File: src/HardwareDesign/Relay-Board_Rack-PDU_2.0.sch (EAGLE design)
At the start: 68 parts, among them IC1 ULN2803A, IC3 TS432ILT, T1 750370228

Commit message: working on Rev2.0
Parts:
- removed CON1: (no value), ds_con:CON-2X7
- added 3V3DC, 5VDC, GND, GND-3, GND-5, SW3, SW5, VFB3, VFB5: TP, ds_passive:TP
- added C1, C2: 100nF, ds_passive:C-0402
- added C36, C40, C42, C48, C49, C51: 100nF, ds_passive:C0402
- added C43, C52: 33pF, ds_passive:C0402
- added C44, C45: 22uF 25V, ds_passive:C-1206
- added C46, C47, C53, C57: 22uF - 10V, ds_passive:C-1206
- added IC2: MCP23017-E/ML, ds_ic_peripherals:MCP23017-E/ML
- added IC5: MP2315S, ds_ic_vreg:MP2315TSOT23-8
- added IC7: MP2315GJ-Z, ds_ic_vreg:MP2315TSOT23-8
- added L1: 4.9uH, ds_passive:L
- added L3: 4.2uH, ds_passive:L
- added R29, R45: 100K, ds_passive:R0402
- added R30, R31: 499K, ds_passive:R0402
- added R32, R37: 7.5K, ds_passive:R0402
- added R33: 9.09K, ds_passive:R0402
- added R34, R41: 10R, ds_passive:R0402
- added R35: 20K, ds_passive:R0402
- added R36, R43: 40.2K, ds_passive:R0402
- added R42: 33K, ds_passive:R0402
- added R44: 12.7K, ds_passive:R0402
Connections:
- removed net I_MEA/TX: CON1.4
- removed net VMEA/RX: CON1.3
- new net EXP_RST: IC2.!RESET
- new net I2C_SCL: IC2.SCL
- new net I2C_SDA: IC2.SDA
- new net N$14: IC7.BST, R34.2
- new net N$16: IC7.FB, R35.1
- new net N$17: C51.2, IC7.SW, L1.1, SW5.P$1
- new net N$18: C51.1, R34.1
- new net N$19: IC7.EN, R31.2
- new net N$21: C49.1, IC7.VCC, R29.1
- new net N$37: C52.2, R35.2, R36.2, R37.1, VFB5.P$1
- new net N$38: IC5.BST, R41.2
- new net N$39: IC5.FB, R42.1
- new net N$40: C42.2, IC5.SW, L3.1, SW3.P$1
- new net N$41: C42.1, R41.1
- new net N$42: C43.2, R42.2, R43.2, R44.1, VFB3.P$1
- new net N$43: IC5.EN, R30.2
- new net N$44: C40.1, IC5.VCC, R45.1
- new net N$45: IC7.AAM, R29.2, R33.1
- new net N$46: IC5.AAM, R32.1, R45.2
- net +12V: now also C36.1, C44.1, C45.1, C48.1, IC5.IN, IC7.IN, R30.1, R31.1; no longer CON1.14
- net +3V3: now also 3V3DC.P$1, C1.1, C2.1, C43.1, C47.1, C57.1, IC2.VDD, L3.2, R43.1; no longer CON1.1
- net +5V: now also 5VDC.P$1, C46.1, C52.1, C53.1, L1.2, R36.1; no longer CON1.2
- net GND: now also C1.2, C2.2, C36.2, C40.2, C44.2, C45.2, C46.2, C47.2, C48.2, C49.2, C53.2, C57.2, GND-3.P$1, GND-5.P$1, GND.P$1, IC2.A0, IC2.A1, IC2.A2, IC2.VSS, IC5.GND, IC7.GND, R32.2, R33.2, R37.2, R44.2; no longer CON1.13
- net REL_0: now also IC2.IO1.0; no longer CON1.12
- net REL_1: now also IC2.IO1.1; no longer CON1.11
- net REL_2: now also IC2.IO1.2; no longer CON1.10
- net REL_3: now also IC2.IO1.3; no longer CON1.9
- net REL_4: now also IC2.IO1.4; no longer CON1.8
- net REL_5: now also IC2.IO1.5; no longer CON1.7
- net REL_6: now also IC2.IO1.6; no longer CON1.6
- net REL_7: now also IC2.IO1.7; no longer CON1.5
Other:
- note added: "3.3V DC-DC CONVERTER"
- note added: "5V DC-DC CONVERTER"
- note added: "IO DRIVER"
- note removed: "DRIVER CONNECTOR"
- moved on the sheet: IC1, R1, R2, R3, R4, R5, R6, R7, R8

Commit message: working on Rev2.0
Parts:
- removed 3V3DC, SW5, VFB3, VFB5: TP, ds_passive:TP
- removed BR1: DBLS207G, ds_active:DBLS207G
- removed C45: 22uF 25V, ds_passive:C-1206
- removed C46, C47, C53, C57: 22uF - 10V, ds_passive:C-1206
- removed C51: 100nF, ds_passive:C0402
- removed C52: 33pF, ds_passive:C0402
- removed CM1: 20mH CM CHOKE, ds_trafo:WE-CMB_XS_744821120
- removed D15: MRA4007T3G, Diodes:SS12
- removed D16: STPS5H100B, ds_active:STPS5H100B
- removed D17, D18, D19: BAT41ZFILM, diode:CGRM4001-G
- removed D20: MMSZ5248B-V-GS08, Diodes-2:BZG03C240-HM3-08
- removed F2: 696101000002, Wurth_Connectors_WR-FSH:696101000002
- removed L3: 4.2uH, ds_passive:L
- removed REL1, REL2, REL3, REL4, REL5, REL6, REL7, REL8: G2RL-1A-E_DC12, ds_passive:G2RL-1A-E_DC12
- removed RV1: B72210S0321K101, Wurth_EMC Components_WE-VD:WE-VD_10MM_820412001
- removed T1: 750370228, ds_trafo:750370228
- added 12VDC, 3VDC, 3VFB, 5VFB, SW: TP, ds_passive:TP
- added AC/DC1: (no value), ds_trafo:IRM_10_12
- added AC_L, AC_N: (no value), con-wago-500:W237-102
- added C10, C13: 100uF, ds_passive:CPOL
- added C11, C12: 33pF, ds_passive:C0402
- added C27, C28, C29, C30, C31, C32, C37, C38, C39, C41, C50, C54, C55, C56: 33nF, ds_passive:C-1206
- added C3, C4, C6, C7, C8, C9: 100nF, ds_passive:C0402
- added C33, C34: 100nF, ds_passive:C-0402
- added C5: 10uF 16V, ds_passive:C-1206
- added D10, D9: S1M, diode:S1M
- added D11: 9.1V 1W, diode:ZENER-DIODESMB
- added IC10, IC11, IC12, IC14, IC16, IC6, IC8: HLW8032, ds_ic_peripherals:HLW8032
- added IC9: SN74HC151PWR, ds_ic_logic:SN74HC151PWR
- added J1: 687320124422, Wurth_Connectors_WR-FPC:6873XX124422_687320124422
- added K1, K2, K3, K4, K5, K6, K7, K8: G2RL-1A-E_DC12, ds_passive:G2RL-1A-E_DC12
- added OPT1: TLP291-4, ds_ic_peripherals:TLP291-4(GB-TP,E)1
- added R100, R101, R102, R103, R116, R117, R118, R119, R38, R39, R46, R47, R52, R53, R54, R55, R68, R69, R70, R71, R76, R77, R78, R79, R84, R85, R86, R87: 470K, ds_passive:R1206
- added R104, R113, R114, R120, R40, R48, R49, R50, R56, R65, R66, R72, R73, R74, R80, R81, R82, R88, R97, R98: 1K 1%, ds_passive:R1206
- added R11: 40.2K, ds_passive:R0402
- added R115, R25, R26, R27, R28, R51, R67, R75, R83, R99: 0.002R 1%, ds_passive:R2512
- added R12: 7.5K, ds_passive:R0402
- added R57, R58, R59: JP, ds_passive:R0402
- added R60: 470K 1W, ds_passive:R2512
- added R61, R62: 100R 1W, ds_passive:R2512
- added R63, R64, R89, R90: 4x1K 1206, Resistor Array:742C083103JP
- added R91, R92: 0R, ds_passive:R0402
- added R93: 4x10K 1206, Resistor Array:742C083103JP
- added R94: 100K, ds_passive:R0402
- added R95: 10K, ds_passive:R0402
- added Z1: SMAJ15A, 52101-101-REV-A_v16:SUPRESSOR_TVS-UD-SMAJ
- C1, C2: value 100nF -> 22uF 25V; device ds_passive:C-0402 -> ds_passive:C-1206
- C14: value MP2104K27C3R6LC 100nF 275V -> 22uF - 10V; device ds_passive:C -> ds_passive:C-1206
- C15, C17: value KM150M400G160A 15uF 400V -> 22uF - 10V; device Capacitor:C-POL_RADIAL-25MM-DIA -> ds_passive:C-1206
- C16: value 1nF 630V -> 100uF; device ds_passive:C-1206 -> ds_passive:CPOL
- C18: value 470uF 25V -> 22uF - 10V; device Capacitor:C-POL_RADIAL-11MM-DIA -> ds_passive:C-1206
- C19: value 100uF 25V -> 100nF; device Capacitor:C-POL_RADIAL-11MM-DIA -> ds_passive:C-0402
- C20: value 1uF 25V -> 100nF; device ds_passive:C-0805 -> ds_passive:C-0402
- C21: value 10nF 50V -> 470nF 630V; device ds_passive:C-0805 -> ds_passive:C-2225
- C22: value 2.2nF 50V -> 470uF 25V; device ds_passive:C-0603 -> ds_passive:CPOL
- C23: value 33nF 16V -> 10uF 16V; device ds_passive:C-0603 -> ds_passive:C-1206
- C24: value 220pF -> 33nF; device ds_passive:C-0805 -> ds_passive:C-1206
- C25: value 33uF 35V -> 33nF; device Capacitor:C-POL_RADIAL-11MM-DIA -> ds_passive:C-1206
- C26: value 2.2nF 250VAC -> 33nF; device ds_passive:C102-1KV -> ds_passive:C-1206
- C36, C40, C42, C48, C49: value 100nF -> 33nF; device ds_passive:C0402 -> ds_passive:C-1206
- C43: value 33pF -> 33nF; device ds_passive:C0402 -> ds_passive:C-1206
- C44: value 22uF 25V -> 33nF
- IC1: value ULN2803A -> MP2315GJ-Z; device ds_ic_peripherals:ULN2803 -> ds_ic_vreg:MP2315TSOT23-8
- IC2: value MCP23017-E/ML -> MP2315S; device ds_ic_peripherals:MCP23017-E/ML -> ds_ic_vreg:MP2315TSOT23-8
- IC3: value TS432ILT -> ULN2803A; device ds_ic_vreg:TS432ILT -> ds_ic_peripherals:ULN2803
- IC4: value (none) -> MCP23017-E/ML; device ds_ic_peripherals:VIPER35HD -> ds_ic_peripherals:MCP23017-E/ML
- IC5: value MP2315S -> BA50BC0FP-E2; device ds_ic_vreg:MP2315TSOT23-8 -> ds_ic_vreg:L4941BDT
- IC7: value MP2315GJ-Z -> HLW8032; device ds_ic_vreg:MP2315TSOT23-8 -> ds_ic_peripherals:HLW8032
- L2: value 3.3uH SD43-332ML -> 4.2uH; device 52101-101-REV-A_v16:INDUCTOR-BOURNS_SRN8040 -> ds_passive:L
- OPT2: value SFH6106-2T -> TLP291-4; device ds_ic_peripherals:SFH6106-3SMD-4_SFH610X_VIS-M -> ds_ic_peripherals:TLP291-4(GB-TP,E)1
- R1, R2: value 330R 1W -> 499K; device ds_passive:R1206 -> ds_passive:R0402
- R10: value 0R -> 33K; device ds_passive:R0805 -> ds_passive:R0402
- R13: value 220K 5% 0.33W 200V -> 40.2K; device ds_passive:R1206 -> ds_passive:R0402
- R14: value 1K -> 12.7K; device ds_passive:R0603 -> ds_passive:R0402
- R15: value 12K -> 0R; device ds_passive:R0603 -> ds_passive:R0805
- R16: value 82K -> 0R; device ds_passive:R0603 -> ds_passive:R0805
- R17: value 130K 1% -> 330R 1W; device ds_passive:R0603 -> ds_passive:R1206
- R18: value 15K 1% -> 330R 1W; device ds_passive:R0603 -> ds_passive:R1206
- R19: value 4.7R 1% -> 330R 1W; device ds_passive:R0603 -> ds_passive:R1206
- R20: value 330K 1% -> 330R 1W; device ds_passive:R0603 -> ds_passive:R1206
- R21: value 133K 1% -> 330R 1W; device ds_passive:R0603 -> ds_passive:R1206
- R22: value 30K 1% -> 330R 1W; device ds_passive:R0603 -> ds_passive:R1206
- R23: value 47K 1% -> 330R 1W; device ds_passive:R0603 -> ds_passive:R1206
- R24: value 220R -> 330R 1W; device ds_passive:R0805 -> ds_passive:R1206
- R29: value 100K -> 0.002R 1%; device ds_passive:R0402 -> ds_passive:R2512
- R3, R5: value 330R 1W -> 100K; device ds_passive:R1206 -> ds_passive:R0402
- R30, R31: value 499K -> 0.002R 1%; device ds_passive:R0402 -> ds_passive:R2512
- R32: value 7.5K -> 0.002R 1%; device ds_passive:R0402 -> ds_passive:R2512
- R33: value 9.09K -> 1K 1%; device ds_passive:R0402 -> ds_passive:R1206
- R34, R41: value 10R -> 1K 1%; device ds_passive:R0402 -> ds_passive:R1206
- R35: value 20K -> 0.002R 1%; device ds_passive:R0402 -> ds_passive:R2512
- R36: value 40.2K -> 470K; device ds_passive:R0402 -> ds_passive:R1206
- R37: value 7.5K -> 470K; device ds_passive:R0402 -> ds_passive:R1206
- R4: value 330R 1W -> 9.09K; device ds_passive:R1206 -> ds_passive:R0402
- R42: value 33K -> 1K 1%; device ds_passive:R0402 -> ds_passive:R1206
- R43: value 40.2K -> 0.002R 1%; device ds_passive:R0402 -> ds_passive:R2512
- R44: value 12.7K -> 470K; device ds_passive:R0402 -> ds_passive:R1206
- R45: value 100K -> 470K; device ds_passive:R0402 -> ds_passive:R1206
- R6: value 330R 1W -> 7.5K; device ds_passive:R1206 -> ds_passive:R0402
- R7: value 330R 1W -> 10R; device ds_passive:R1206 -> ds_passive:R0402
- R8: value 330R 1W -> 20K; device ds_passive:R1206 -> ds_passive:R0402
- R9: value 0R -> 10R; device ds_passive:R0805 -> ds_passive:R0402
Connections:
- removed net AC_LINE: F2.1, REL1.3, REL1.6, REL2.3, REL2.6, REL3.3, REL3.6, REL4.3, REL4.6, REL5.3, REL5.6, REL6.3, REL6.6, REL7.3, REL7.6, REL8.3, REL8.6
- removed net AC_LINE2: C14.2, CM1.1, RV1.2
- removed net DC_RAW: BR1.+, C15.+, C16.1, C17.+, R13.2, T1.6
- removed net EXP_RST: IC2.!RESET
- removed net FB: C22.1, C23.1, IC4.FB, OPT2.3
- new net +12V_MEA: J1.13, R94.1, R95.2
- new net +5V_MEA: C23.1, C5.1, IC10.VDD, IC11.VDD, IC12.VDD, IC14.VDD, IC16.VDD, IC5.VOUT, IC6.VDD, IC7.VDD, IC8.VDD, R63.1, R63.2, R63.3, R63.4, R64.1, R64.2, R64.3, R64.4
- new net 5VFB: 5VFB.P$1, C11.2, R11.2, R12.1, R8.2
- new net AC_L: AC/DC1.AC/L, AC_L-1.KL, AC_L-2.KL, C21.1, K1.3, K1.6, K2.3, K2.6, K3.3, K3.6, K4.3, K4.6, K5.3, K5.6, K6.3, K6.6, K7.3, K7.6, K8.3, K8.6, R60.1
- new net AC_N: AC/DC1.AC/N, AC_N-1.KL, AC_N-2.KL, R57.1, R58.1, R59.1
- new net C13_IN1: R25.2, R33.1, R35.2
- new net C13_IN2: R32.2, R49.1, R51.2
- new net C13_IN3: R31.2, R65.1, R67.2
- new net C13_IN4: R30.2, R81.1, R83.2
- new net C13_IN5: R26.2, R41.1, R43.2
- new net C13_IN6: R27.2, R73.1, R75.2
- new net C13_IN7: R28.2, R97.1, R99.2
- new net C13_IN8: R113.1, R115.2, R29.2
- new net MCP_REL_RST: IC4.!RESET, J1.15
- new net MUX_A: IC4.IO2.0, IC9.A, R93.4
- new net MUX_B: IC4.IO2.1, IC9.B, R93.3
- new net MUX_C: IC4.IO2.2, IC9.C, R93.2
- new net MUX_EN: IC4.IO2.3, IC9.!EN, R93.1
- new net N$1: IC9.Y, R91.1
- new net N$100: C56.1, IC16.VP, R119.2, R120.1
- new net N$3: C21.2, R60.2, R61.1
- new net N$4: IC3.5C, R21.1
- new net N$47: C30.1, IC8.INP, R49.2
- new net N$48: C31.1, IC8.INN, R50.2
- new net N$49: R52.2, R53.1
- new net N$50: R53.2, R54.1
- new net N$51: R54.2, R55.1
- new net N$52: C32.1, IC8.VP, R55.2, R56.1
- new net N$53: OPT2.5, R64.6
- new net N$54: OPT2.7, R64.5
- new net N$59: C36.1, IC10.INP, R65.2
- new net N$60: C37.1, IC10.INN, R66.2
- new net N$61: R68.2, R69.1
- new net N$62: R69.2, R70.1
- new net N$63: R70.2, R71.1
- new net N$64: C38.1, IC10.VP, R71.2, R72.1
- new net N$65: C39.1, IC11.INP, R73.2
- new net N$66: C40.1, IC11.INN, R74.2
- new net N$67: R76.2, R77.1
- new net N$68: R77.2, R78.1
- new net N$69: R78.2, R79.1
- new net N$70: C41.1, IC11.VP, R79.2, R80.1
- new net N$71: C42.1, IC12.INP, R81.2
- new net N$72: C43.1, IC12.INN, R82.2
- new net N$73: R84.2, R85.1
- new net N$74: R85.2, R86.1
- new net N$75: R86.2, R87.1
- new net N$76: C44.1, IC12.VP, R87.2, R88.1
- new net N$83: C48.1, IC14.INP, R97.2
- new net N$84: C49.1, IC14.INN, R98.2
- new net N$85: R100.2, R101.1
- new net N$86: R101.2, R102.1
- new net N$87: R102.2, R103.1
- new net N$88: C50.1, IC14.VP, R103.2, R104.1
- new net N$95: C54.1, IC16.INP, R113.2
- new net N$96: C55.1, IC16.INN, R114.2
- new net N$97: R116.2, R117.1
- new net N$98: R117.2, R118.1
- new net N$99: R118.2, R119.1
- new net RX_CH1: IC6.RX
- new net RX_CH2: IC8.RX
- new net RX_CH3: IC10.RX
- new net RX_CH4: IC12.RX
- new net RX_CH5: IC7.RX
- new net RX_CH6: IC11.RX
- new net RX_CH7: IC14.RX
- new net RX_CH8: IC16.RX
- new net SW3: C9.2, IC2.SW, L2.1, SW3.P$1
- new net SW5: C8.2, IC1.SW, L1.1, SW.P$1
- new net TX_CH1: IC6.TX, OPT1.2
- new net TX_CH2: IC8.TX, OPT1.4
- new net TX_CH3: IC10.TX, OPT1.6
- new net TX_CH4: IC12.TX, OPT1.8
- new net TX_CH5: IC7.TX, OPT2.2
- new net TX_CH6: IC11.TX, OPT2.4
- new net TX_CH7: IC14.TX, OPT2.6
- new net TX_CH8: IC16.TX, OPT2.8
- new net TX_MUX1: IC9.D0, OPT1.16, R89.1
- new net TX_MUX2: IC9.D1, OPT1.14, R89.2
- new net TX_MUX3: IC9.D2, OPT1.12, R89.3
- new net TX_MUX4: IC9.D3, OPT1.10, R89.4
- new net TX_MUX5: IC9.D4, OPT2.16, R90.1
- new net TX_MUX6: IC9.D5, OPT2.14, R90.2
- new net TX_MUX7: IC9.D6, OPT2.12, R90.3
- new net TX_MUX8: IC9.D7, OPT2.10, R90.4
- new net UART0_RX: J1.10
- new net UART0_TX: J1.11, R91.2, R92.2
- net +12V: now also C1.1, C2.1, C3.1, C4.1, IC1.IN, IC2.IN, IC3.COM, K1.8, K2.8, K3.8, K4.8, K5.8, K6.8, K7.8, K8.8, R1.1, R15.1, R16.1, R2.1, R94.2; no longer C36.1, C44.1, C45.1, C48.1, IC1.COM, IC5.IN, IC7.IN, R10.1, R30.1, R31.1, R9.1, REL1.8, REL2.8, REL3.8, REL4.8, REL5.8, REL6.8, REL7.8, REL8.8
- net +3V3: now also 3VDC.P$1, C12.1, C15.1, C18.1, C19.1, C20.1, C33.1, C34.1, IC4.VDD, IC9.VCC, J1.4, J1.5, J1.6, L2.2, R13.1, R89.5, R89.6, R89.7, R89.8, R90.5, R90.6, R90.7, R90.8, R93.5, R93.6, R93.7, R93.8; no longer 3V3DC.P$1, C1.1, C2.1, C43.1, C47.1, C57.1, IC2.VDD, L3.2, R43.1
- net +5V: now also C11.1, C14.1, C17.1, J1.1, J1.2, J1.3, R11.1; no longer C46.1, C52.1, C53.1, R36.1
- net AGND: now also C23.2, C25.2, C26.2, C27.2, C28.2, C29.2, C30.2, C31.2, C32.2, C36.2, C37.2, C38.2, C39.2, C40.2, C41.2, C42.2, C43.2, C44.2, C48.2, C49.2, C5.2, C50.2, C54.2, C55.2, C56.2, D10.A, D11.A, IC10.GND, IC11.GND, IC12.GND, IC14.GND, IC16.GND, IC5.GND, IC6.GND, IC7.GND, IC8.GND, R104.2, R120.2, R40.2, R48.2, R56.2, R57.2, R58.2, R59.2, R72.2, R80.2, R88.2; no longer BR1.-, C15.-, C17.-, C25.-, C26.1, D17.A, D20.A, IC4.BR, IC4.GND, OPT2.4, R22.2, R23.2, T1.3
- net GND: now also AC/DC1.-V, C10.2, C13.2, C14.2, C15.2, C16.2, C17.2, C18.2, C19.2, C3.2, C33.2, C34.2, C4.2, C6.2, C7.2, IC2.GND, IC3.GND, IC4.A0, IC4.A1, IC4.A2, IC4.VSS, IC9.GND, J1.12, J1.14, J1.16, J1.9, J1.Z1, J1.Z2, J1.Z3, J1.Z4, OPT1.11, OPT1.13, OPT1.15, OPT1.9, OPT2.11, OPT2.13, OPT2.15, OPT2.9, R12.2, R14.2, R4.2, R6.2, R95.1, Z1.A; no longer C18.-, C19.-, C26.2, C36.2, C40.2, C44.2, C45.2, C46.2, C47.2, C48.2, C49.2, C53.2, C57.2, IC2.A0, IC2.A1, IC2.A2, IC2.VSS, IC3.3, IC5.GND, IC7.GND, R18.2, R32.2, R33.2, R37.2, R44.2, T1.10
- net I2C_SCL: now also IC4.SCL, J1.8; no longer IC2.SCL
- net I2C_SDA: now also IC4.SDA, J1.7; no longer IC2.SDA
- net N$10: now also IC3.4C, R20.1; no longer IC1.5C, R5.1
- net N$11: now also IC3.3C, R19.1; no longer IC1.6C, R6.1
- net N$12: now also C24.1, IC6.INP, R33.2; no longer BR1.AC2, CM1.3
- net N$13: now also IC3.2C, R18.1; no longer IC1.7C, R7.1
- net N$14: now also IC1.BST, R7.2; no longer IC7.BST, R34.2
- net N$15: now also IC3.1C, R17.1; no longer IC1.8C, R8.1
- net N$16: now also IC1.FB, R8.1; no longer IC7.FB, R35.1
- net N$17: now also OPT1.5, R63.6; no longer C51.2, IC7.SW, L1.1, SW5.P$1
- net N$18: now also C8.1, R7.1; no longer C51.1, R34.1
- net N$19: now also IC1.EN, R1.2; no longer IC7.EN, R31.2
- net N$2: now also 12VDC.P$1, AC/DC1.+V, C10.1, C13.1, C16.1, R15.2, R16.2, Z1.C; no longer C19.+, C20.1, L2.2, R10.2, R17.1, R9.2
- net N$20: now also D10.C, D9.A, R61.2; no longer C14.1, CM1.2, F2.2, RV1.1
- net N$21: now also C6.1, IC1.VCC, R3.1; no longer C49.1, IC7.VCC, R29.1
- net N$22: now also C25.1, IC6.INN, R34.2; no longer C16.2, D15.C, R13.1
- net N$23: now also OPT1.7, R63.5; no longer D15.A, IC4.DRAIN, T1.4
- net N$24: now also IC9.!Y, R92.1; no longer D16.2, T1.8
- net N$25: now also C22.1, IC5.VIN, R62.2; no longer C18.+, D16.3, L2.1, R14.1
- net N$26: now also D11.C, D9.C, R62.1; no longer IC3.2, OPT2.1, R14.2, R15.1
- net N$27: now also R36.2, R37.1; no longer OPT2.2, R15.2, R16.1
- net N$28: now also R37.2, R38.1; no longer C21.1, R16.2
- net N$29: now also R38.2, R39.1; no longer C21.2, IC3.1, R17.2, R18.1
- net N$30: now also C26.1, IC6.VP, R39.2, R40.1; no longer C24.1, C25.+, D19.C, IC4.VDD, R24.1
- net N$31: now also C27.1, IC7.INP, R41.2; no longer D19.A, R19.2
- net N$32: now also C28.1, IC7.INN, R42.2; no longer D18.A, R19.1, R20.1, T1.1
- net N$33: now also R44.2, R45.1; no longer D17.C, D18.C, R21.1
- net N$34: now also R45.2, R46.1; no longer IC4.ZCD, R20.2, R21.2, R22.1
- net N$35: now also R46.2, R47.1; no longer C23.2, R23.1
- net N$36: now also C29.1, IC7.VP, R47.2, R48.1; no longer D20.C, R24.2
- net N$37: now also OPT2.1, R64.8; no longer C52.2, R35.2, R36.2, R37.1, VFB5.P$1
- net N$38: now also IC2.BST, R9.2; no longer IC5.BST, R41.2
- net N$39: now also IC2.FB, R10.1; no longer IC5.FB, R42.1
- net N$40: now also OPT2.3, R64.7; no longer C42.2, IC5.SW, L3.1, SW3.P$1
- net N$41: now also C9.1, R9.1; no longer C42.1, R41.1
- net N$42: now also 3VFB.P$1, C12.2, R10.2, R13.2, R14.1; no longer C43.2, R42.2, R43.2, R44.1, VFB3.P$1
- net N$43: now also IC2.EN, R2.2; no longer IC5.EN, R30.2
- net N$44: now also C7.1, IC2.VCC, R5.1; no longer C40.1, IC5.VCC, R45.1
- net N$45: now also IC1.AAM, R3.2, R4.1; no longer IC7.AAM, R29.2, R33.1
- net N$46: now also IC2.AAM, R5.2, R6.1; no longer IC5.AAM, R32.1, R45.2
- net N$5: now also OPT1.1, R63.8; no longer BR1.AC1, CM1.4
- net N$6: now also IC3.8C, R24.1; no longer IC1.1C, R1.1
- net N$7: now also IC3.7C, R23.1; no longer IC1.2C, R2.1
- net N$8: now also IC3.6C, R22.1; no longer IC1.3C, R3.1
- net N$9: now also OPT1.3, R63.7; no longer IC1.4C, R4.1
- net OUT_1: now also K1.4, K1.5, R25.1, R34.1, R35.1, R36.1; no longer REL1.4, REL1.5
- net OUT_2: now also K2.4, K2.5, R32.1, R50.1, R51.1, R52.1; no longer REL2.4, REL2.5
- net OUT_3: now also K3.4, K3.5, R31.1, R66.1, R67.1, R68.1; no longer REL3.4, REL3.5
- net OUT_4: now also K4.4, K4.5, R30.1, R82.1, R83.1, R84.1; no longer REL4.4, REL4.5
- net OUT_5: now also K5.4, K5.5, R26.1, R42.1, R43.1, R44.1; no longer REL5.4, REL5.5
- net OUT_6: now also K6.4, K6.5, R27.1, R74.1, R75.1, R76.1; no longer REL6.4, REL6.5
- net OUT_7: now also K7.4, K7.5, R100.1, R28.1, R98.1, R99.1; no longer REL7.4, REL7.5
- net OUT_8: now also K8.4, K8.5, R114.1, R115.1, R116.1, R29.1; no longer REL8.4, REL8.5
- net RELAY_1: now also K1.1, R24.2; no longer R1.2, REL1.1
- net RELAY_2: now also K2.1, R23.2; no longer R2.2, REL2.1
- net RELAY_3: now also K3.1, R22.2; no longer R3.2, REL3.1
- net RELAY_4: now also K4.1, R21.2; no longer R4.2, REL4.1
- net RELAY_5: now also K5.1, R20.2; no longer R5.2, REL5.1
- net RELAY_6: now also K6.1, R19.2; no longer R6.2, REL6.1
- net RELAY_7: now also K7.1, R18.2; no longer R7.2, REL7.1
- net RELAY_8: now also K8.1, R17.2; no longer R8.2, REL8.1
- net REL_0: now also IC3.8B, IC4.IO1.0; no longer IC1.1B, IC2.IO1.0
- net REL_1: now also IC3.7B, IC4.IO1.1; no longer IC1.2B, IC2.IO1.1
- net REL_2: now also IC3.6B, IC4.IO1.2; no longer IC1.3B, IC2.IO1.2
- net REL_3: now also IC3.5B, IC4.IO1.3; no longer IC1.4B, IC2.IO1.3
- net REL_4: now also IC3.4B, IC4.IO1.4; no longer IC1.5B, IC2.IO1.4
- net REL_5: now also IC3.3B, IC4.IO1.5; no longer IC1.6B, IC2.IO1.5
- net REL_6: now also IC3.2B, IC4.IO1.6; no longer IC1.7B, IC2.IO1.6
- net REL_7: now also IC3.1B, IC4.IO1.7; no longer IC1.8B, IC2.IO1.7
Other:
- note added: "12V - 10W FLYBACK CONVERTER"
- note added: "5V AC-MEASUREMENT"
- note added: "AC CHANNEL MEASUREMENT"
- note added: "BOARD CONNECTOR"
- note added: "SERIAL MUX"
- note added: "SERIAL OPTOISOLATOR"
- note removed: "12 V - 15 W FLYBACK CONVERTER"

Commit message: finished with design update for 2.0
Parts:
- J1: value 687320124422 -> FPC20-H; device Wurth_Connectors_WR-FPC:6873XX124422_687320124422 -> ds_con:FPC20-H
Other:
- moved on the sheet: J1
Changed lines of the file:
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@@
 <part name="+3V5" library="ds_passive" deviceset="+3V3" device=""/>
 <part name="R93" library="Resistor Array" library_urn="urn:adsk.eagle:library:16491332" deviceset="742C083103JP" device="" package3d_urn="urn:adsk.eagle:package:16445849/4" value="4x10K 1206"/>
-<part name="J1" library="Wurth_Connectors_WR-FPC" library_urn="urn:adsk.eagle:library:15778639" deviceset="6873XX124422_687320124422" device="" package3d_urn="urn:adsk.eagle:package:15743882/4" value="687320124422"/>
+<part name="J1" library="ds_con" deviceset="FPC20-H" device="" package3d_urn="urn:adsk.eagle:package:47082459/2" value="FPC20-H"/>
 <part name="GND29" library="ds_passive" deviceset="GND" device=""/>
 <part name="+3V6" library="ds_passive" deviceset="+3V3" device=""/>
@@
 <attribute name="VALUE" x="106.68" y="56.134" size="1.778" layer="96"/>
 </instance>
-<instance part="J1" gate="G$1" x="307.34" y="68.58" smashed="yes" rot="MR270">
-<attribute name="NAME" x="304.292" y="69.85" size="1.27" layer="95" rot="MR270" align="bottom-center"/>
-<attribute name="VALUE" x="304.292" y="56.388" size="1.27" layer="96" rot="MR270"/>
+<instance part="J1" gate="G$1" x="304.8" y="68.58" smashed="yes">
+<attribute name="NAME" x="303.53" y="71.628" size="1.27" layer="95" align="bottom-center"/>
 </instance>
 <instance part="GND29" gate="1" x="314.96" y="33.02" smashed="yes">
@@
 </segment>
 <segment>
-<wire x1="304.8" y1="99.06" x2="304.8" y2="101.6" width="0.1524" layer="91"/>
-<wire x1="304.8" y1="101.6" x2="307.34" y2="101.6" width="0.1524" layer="91"/>
-<wire x1="307.34" y1="101.6" x2="314.96" y2="101.6" width="0.1524" layer="91"/>
-<wire x1="314.96" y1="101.6" x2="314.96" y2="73.66" width="0.1524" layer="91"/>
-<wire x1="314.96" y1="73.66" x2="314.96" y2="66.04" width="0.1524" layer="91"/>
-<wire x1="314.96" y1="66.04" x2="314.96" y2="60.96" width="0.1524" layer="91"/>
-<wire x1="314.96" y1="60.96" x2="314.96" y2="55.88" width="0.1524" layer="91"/>
+<pinref part="GND29" gate="1" pin="GND"/>
+<pinref part="J1" gate="G$1" pin="16"/>
+<wire x1="312.42" y1="55.88" x2="314.96" y2="55.88" width="0.1524" layer="91"/>
 <wire x1="314.96" y1="55.88" x2="314.96" y2="38.1" width="0.1524" layer="91"/>
 <wire x1="314.96" y1="38.1" x2="314.96" y2="35.56" width="0.1524" layer="91"/>
+<junction x="314.96" y="38.1"/>
+<pinref part="J1" gate="G$1" pin="Z3"/>
 <wire x1="307.34" y1="40.64" x2="307.34" y2="38.1" width="0.1524" layer="91"/>
 <wire x1="307.34" y1="38.1" x2="314.96" y2="38.1" width="0.1524" layer="91"/>
-<junction x="314.96" y="38.1"/>
+<junction x="307.34" y="38.1"/>
+<pinref part="J1" gate="G$1" pin="Z4"/>
 <wire x1="304.8" y1="40.64" x2="304.8" y2="38.1" width="0.1524" layer="91"/>
 <wire x1="304.8" y1="38.1" x2="307.34" y2="38.1" width="0.1524" layer="91"/>
-<junction x="307.34" y="38.1"/>
+<wire x1="304.8" y1="99.06" x2="304.8" y2="101.6" width="0.1524" layer="91"/>
+<wire x1="304.8" y1="101.6" x2="307.34" y2="101.6" width="0.1524" layer="91"/>
+<wire x1="307.34" y1="101.6" x2="314.96" y2="101.6" width="0.1524" layer="91"/>
+<wire x1="314.96" y1="101.6" x2="314.96" y2="73.66" width="0.1524" layer="91"/>
+<wire x1="314.96" y1="73.66" x2="314.96" y2="66.04" width="0.1524" layer="91"/>
 <wire x1="307.34" y1="99.06" x2="307.34" y2="101.6" width="0.1524" layer="91"/>
 <junction x="307.34" y="101.6"/>
 <pinref part="J1" gate="G$1" pin="Z1"/>
 <pinref part="J1" gate="G$1" pin="Z2"/>
-<pinref part="J1" gate="G$1" pin="Z3"/>
-<pinref part="J1" gate="G$1" pin="Z4"/>
-<pinref part="GND29" gate="1" pin="GND"/>
 <pinref part="J1" gate="G$1" pin="9"/>
 <wire x1="312.42" y1="73.66" x2="314.96" y2="73.66" width="0.1524" layer="91"/>
@@
 <pinref part="J1" gate="G$1" pin="12"/>
 <wire x1="312.42" y1="66.04" x2="314.96" y2="66.04" width="0.1524" layer="91"/>
+<wire x1="314.96" y1="66.04" x2="314.96" y2="60.96" width="0.1524" layer="91"/>
 <junction x="314.96" y="66.04"/>
+<junction x="314.96" y="55.88"/>
 <pinref part="J1" gate="G$1" pin="14"/>
+<wire x1="314.96" y1="60.96" x2="314.96" y2="55.88" width="0.1524" layer="91"/>
 <wire x1="312.42" y1="60.96" x2="314.96" y2="60.96" width="0.1524" layer="91"/>
 <junction x="314.96" y="60.96"/>
-<pinref part="J1" gate="G$1" pin="16"/>
-<wire x1="312.42" y1="55.88" x2="314.96" y2="55.88" width="0.1524" layer="91"/>
-<junction x="314.96" y="55.88"/>
 </segment>
 </net>

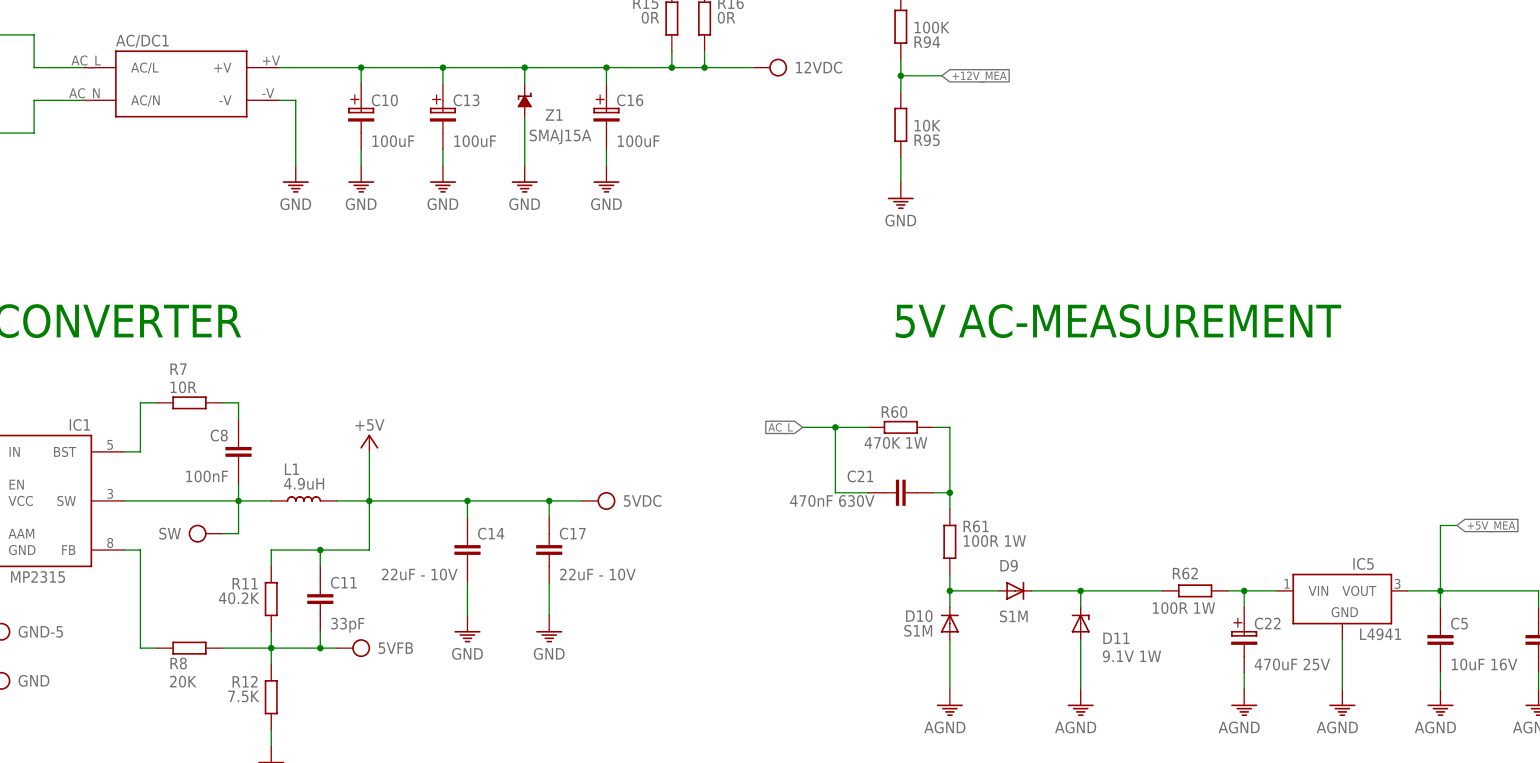
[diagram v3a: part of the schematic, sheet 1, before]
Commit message: add datasheets for Rev2.0
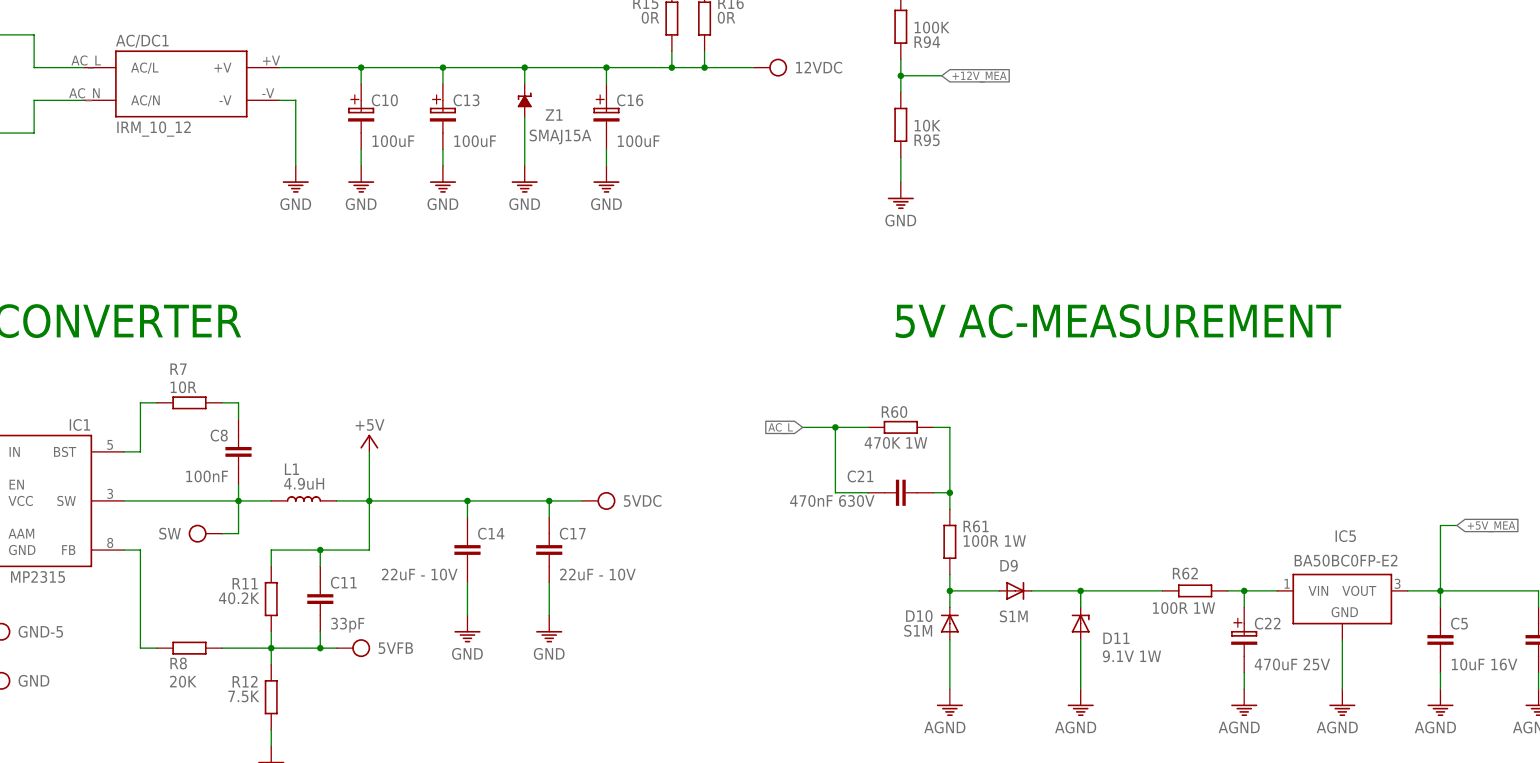
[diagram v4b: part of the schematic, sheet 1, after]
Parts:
- AC/DC1: value (none) -> IRM_10_12
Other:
- note added: "BA50BC0FP-E2"
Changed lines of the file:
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@@
 <part name="IC4" library="ds_ic_peripherals" deviceset="MCP23017" device="-E/ML" package3d_urn="urn:adsk.eagle:package:46683895/2"/>
 <part name="NC2" library="ds_passive" library_urn="urn:adsk.eagle:library:46685041" deviceset="NC" device=""/>
-<part name="AC/DC1" library="ds_trafo" deviceset="IRM_10_12" device="" package3d_urn="urn:adsk.eagle:package:47075710/2"/>
+<part name="AC/DC1" library="ds_trafo" deviceset="IRM_10_12" device="" package3d_urn="urn:adsk.eagle:package:47075710/2" value="IRM_10_12"/>
 <part name="Z1" library="52101-101-REV-A_v16" library_urn="urn:adsk.eagle:library:21899384" deviceset="SUPRESSOR_TVS-UD-" device="SMAJ" package3d_urn="urn:adsk.eagle:package:15662277/2" value="SMAJ15A"/>
 <part name="C10" library="ds_passive" deviceset="CPOL" device="" package3d_urn="urn:adsk.eagle:package:46684204/2" value="100uF"/>
@@
 <text x="87.63" y="82.55" size="5.08" layer="91">3.3V DC-DC CONVERTER</text>
 <text x="260.35" y="166.37" size="5.08" layer="91">5V AC-MEASUREMENT</text>
+<text x="322.58" y="130.81" size="1.778" layer="96">BA50BC0FP-E2</text>
 </plain>
 <instances>
@@
 </instance>
 <instance part="IC5" gate="G$1" x="330.2" y="127" smashed="yes">
-<attribute name="NAME" x="335.28" y="132.08" size="1.778" layer="95" rot="R180"/>
+<attribute name="NAME" x="328.93" y="134.62" size="1.778" layer="95"/>
 </instance>
 <instance part="D9" gate="G$1" x="279.4" y="127" smashed="yes">
